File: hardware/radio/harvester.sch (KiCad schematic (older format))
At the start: 31 parts, among them U201 LTC3331

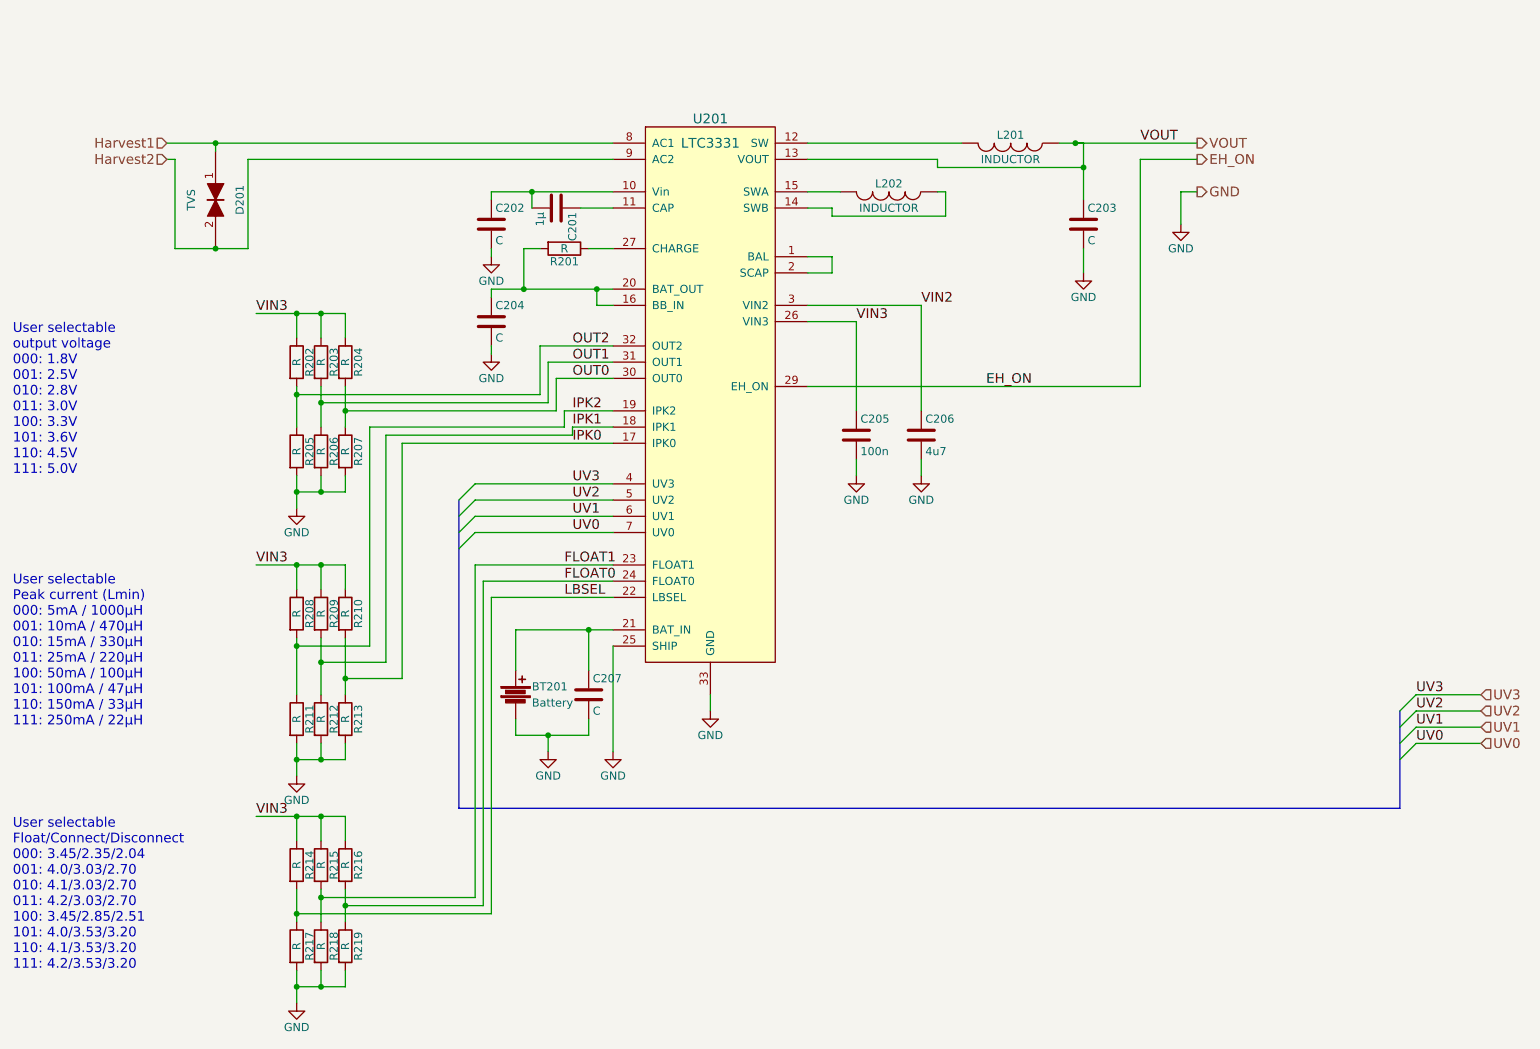
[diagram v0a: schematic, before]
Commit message: Add test points for current and voltage
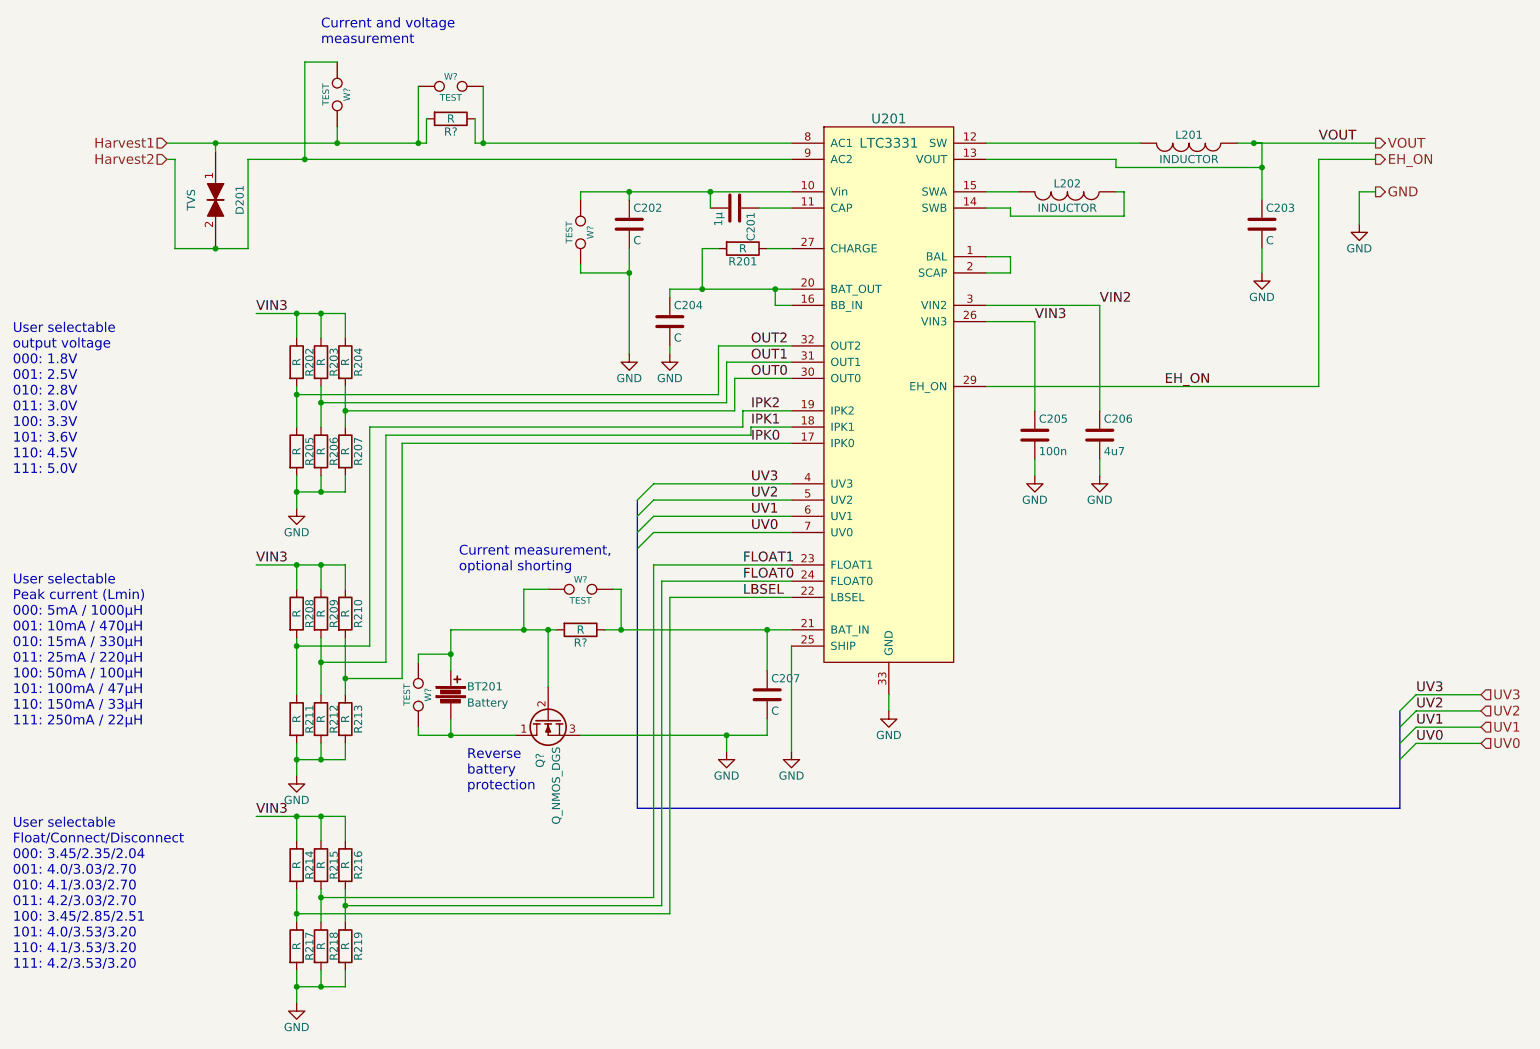
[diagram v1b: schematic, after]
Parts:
- added Q?: Q_NMOS_DGS, symbol Q_NMOS_DGS
- added R? (x2): R, symbol R
- added W? (x5): TEST, symbol TEST
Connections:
- net GND: now also Q?.3 (S), W?.2; no longer BT201.2
- net Harvest1: now also R?.2, W?.1, W?.2; no longer U201.8 (AC1)
- net Harvest2: now also W?.1
- net at C201.2, C202.1, U201.10 (Vin): now also W?.1
- net at C207.1, U201.21 (BAT_IN): now also R?.1, W?.2; no longer BT201.1
- new net: R?.1, U201.8 (AC1), W?.2
- new net: BT201.1, Q?.2 (G), R?.2, W?.1, W?.1
- new net: BT201.2, Q?.1 (D), W?.2
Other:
- note added: "Current and voltage \nmeasurement"
- note added: "Current measurement, \noptional shorting"
- note added: "Reverse \nbattery \nprotection"
- moved on the sheet: BT201, C201, C202, C203, C204, C205, C206, C207, L201, L202, R201, U201

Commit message: Assign testpoint footprints
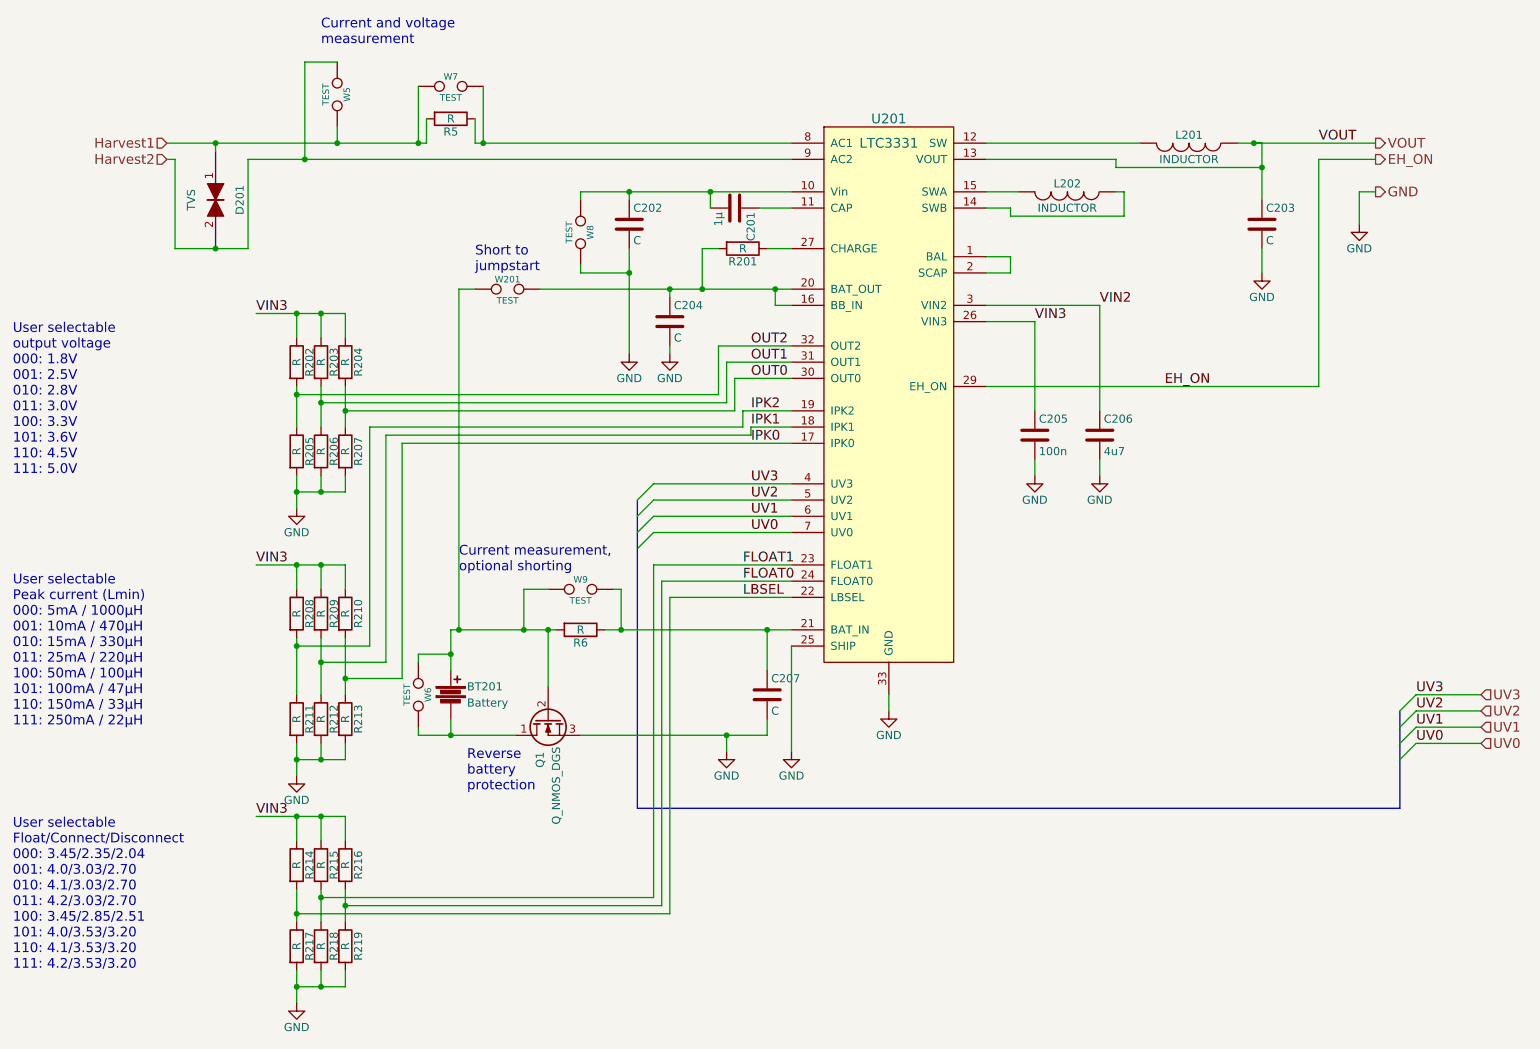
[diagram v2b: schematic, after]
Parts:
- added W201: TEST, footprints_:Test_pair_TH_small, symbol TEST
- BT201: footprint (none) -> footprints_:BLE113
- C201, C202, C203, C204, C205, C206, C207: footprint (none) -> Capacitors_SMD:C_0603
- D201: footprint (none) -> Diodes_SMD:SOD-323
- L201, L202: footprint (none) -> Resistors_SMD:R_1206
- R201, R202, R203, R204, R205, R206, R207, R208, R209, R210, R211, R212, R213, R214, R215, R216, R217, R218, R219, U201: footprint (none) -> Resistors_SMD:R_0603
- R5, R6: renamed from R?; footprint (none) -> Resistors_SMD:R_0603
- W5, W6, W8: renamed from W?; footprint (none) -> footprints_:Test_pair_TH_tiny
- W7, W9: renamed from W?; footprint (none) -> footprints_:Test_pair_TH_small
- gave numbers to parts that had none: 1
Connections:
- net at C204.1, R201.2, U201.16 (BB_IN)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: now also W201.2
- net at BT201.1, Q1.2 (G), R6.2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: now also W201.1
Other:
- note added: "Short to\njumpstart"

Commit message: Assign Q1 footprint
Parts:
- Q1: footprint (none) -> TO_SOT_Packages_SMD:SOT-23
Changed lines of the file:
@@
 F 0 "Q1" H 4700 5800 50  0000 R CNN
 F 1 "Q_NMOS_DGS" H 5050 5700 50  0000 R CNN
-F 2 "" H 4600 5850 29  0001 C CNN
+F 2 "TO_SOT_Packages_SMD:SOT-23" H 4600 5850 29  0001 C CNN
 F 3 "" H 4400 5750 60  0000 C CNN
 	1    4400 5750

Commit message: Parts placed
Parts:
- removed W5: TEST, footprints_:Test_pair_TH_tiny, symbol TEST

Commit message: Change inductor footprints to 1210
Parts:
- BT201: footprint footprints_:BLE113 -> footprints_:CR2032-holder-S8421R
- L201, L202: footprint Resistors_SMD:R_1206 -> Resistors_SMD:R_1210
- U201: footprint Resistors_SMD:R_0603 -> Housings_DFN_QFN:QFN-32-1EP_5x5mm_Pitch0.5mm
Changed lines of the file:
@@
 F 0 "U201" H 6500 4350 60  0000 C CNN
 F 1 "LTC3331" H 6500 4200 60  0000 C CNN
-F 2 "Resistors_SMD:R_0603" H 6500 1750 60  0001 C CNN
+F 2 "Housings_DFN_QFN:QFN-32-1EP_5x5mm_Pitch0.5mm" H 6500 1750 60  0001 C CNN
 F 3 "" H 6500 1750 60  0000 C CNN
 	1    6500 3200
@@
 F 0 "L202" V 7550 2500 50  0000 C CNN
 F 1 "INDUCTOR" V 7700 2500 50  0000 C CNN
-F 2 "Resistors_SMD:R_1206" H 7600 2500 60  0001 C CNN
+F 2 "Resistors_SMD:R_1210" H 7600 2500 60  0001 C CNN
 F 3 "" H 7600 2500 60  0000 C CNN
 	1    7600 2500
@@
 F 0 "L201" V 8300 2200 50  0000 C CNN
 F 1 "INDUCTOR" V 8450 2200 50  0000 C CNN
-F 2 "Resistors_SMD:R_1206" H 8350 2200 60  0001 C CNN
+F 2 "Resistors_SMD:R_1210" H 8350 2200 60  0001 C CNN
 F 3 "" H 8350 2200 60  0000 C CNN
 	1    8350 2200
@@
 F 0 "BT201" H 3900 5650 50  0000 L CNN
 F 1 "Battery" H 3900 5550 50  0000 L CNN
-F 2 "footprints_:BLE113" V 3800 5640 60  0001 C CNN
+F 2 "footprints_:CR2032-holder-S8421R" V 3800 5640 60  0001 C CNN
 F 3 "" V 3800 5640 60  0000 C CNN
 	1    3800 5600

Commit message: Routing finalized
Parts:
- removed Q1: Q_NMOS_DGS, TO_SOT_Packages_SMD:SOT-23, symbol Q_NMOS_DGS
- added Q201: BSH105, symbol Q_NMOS_GSD
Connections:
- net GND: now also Q201.2 (S)
- net VIN3: no longer R214.1, R215.1, R216.1
- net BB_IN: now reaches C204.1, R201.2, U201.16 (BB_IN), U201.20 (BAT_OUT), W201.2
- net BB_IN: now also R214.1, R215.1, R216.1
- net at BT201.1, R6.2, W201.1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: now also Q201.1 (G)
- net at BT201.2, W6.2: now also Q201.3 (D)
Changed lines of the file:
@@
 $EndComp
 $Comp
-L GND #PWR014
+L GND #PWR013
 U 1 1 55E9B04F
 P 4900 3500
-F 0 "#PWR014" H 4900 3250 50  0001 C CNN
+F 0 "#PWR013" H 4900 3250 50  0001 C CNN
 F 1 "GND" H 4900 3350 50  0000 C CNN
 F 2 "" H 4900 3500 60  0000 C CNN
@@
 $EndComp
 $Comp
-L GND #PWR015
+L GND #PWR014
 U 1 1 55E9B130
 P 5150 3500
-F 0 "#PWR015" H 5150 3250 50  0001 C CNN
+F 0 "#PWR014" H 5150 3250 50  0001 C CNN
 F 1 "GND" H 5150 3350 50  0000 C CNN
 F 2 "" H 5150 3500 60  0000 C CNN
@@
 VIN3
 $Comp
-L GND #PWR016
+L GND #PWR015
 U 1 1 55E9B68B
 P 2850 4450
-F 0 "#PWR016" H 2850 4200 50  0001 C CNN
+F 0 "#PWR015" H 2850 4200 50  0001 C CNN
 F 1 "GND" H 2850 4300 50  0000 C CNN
 F 2 "" H 2850 4450 60  0000 C CNN
@@
 	1    0    0    -1
 $EndComp
-Text Label 2600 6350 0    60   ~ 0
-VIN3
-$Comp
-L GND #PWR017
+$Comp
+L GND #PWR016
 U 1 1 55E9C430
 P 2850 7500
-F 0 "#PWR017" H 2850 7250 50  0001 C CNN
+F 0 "#PWR016" H 2850 7250 50  0001 C CNN
 F 1 "GND" H 2850 7350 50  0000 C CNN
 F 2 "" H 2850 7500 60  0000 C CNN
@@
 $EndComp
 $Comp
-L GND #PWR018
+L GND #PWR017
 U 1 1 55E9C656
 P 5900 5950
-F 0 "#PWR018" H 5900 5700 50  0001 C CNN
+F 0 "#PWR017" H 5900 5700 50  0001 C CNN
 F 1 "GND" H 5900 5800 50  0000 C CNN
 F 2 "" H 5900 5950 60  0000 C CNN
@@
 VIN3
 $Comp
-L GND #PWR019
+L GND #PWR018
 U 1 1 55E9DB9C
 P 2850 6100
-F 0 "#PWR019" H 2850 5850 50  0001 C CNN
+F 0 "#PWR018" H 2850 5850 50  0001 C CNN
 F 1 "GND" H 2850 5950 50  0000 C CNN
 F 2 "" H 2850 6100 60  0000 C CNN
@@
 UV0
 $Comp
-L GND #PWR020
+L GND #PWR019
 U 1 1 55E9FF2E
 P 6500 5700
-F 0 "#PWR020" H 6500 5450 50  0001 C CNN
+F 0 "#PWR019" H 6500 5450 50  0001 C CNN
 F 1 "GND" H 6500 5550 50  0000 C CNN
 F 2 "" H 6500 5700 60  0000 C CNN
@@
 $EndComp
 $Comp
-L GND #PWR021
+L GND #PWR020
 U 1 1 55EA0A97
 P 8800 3000
-F 0 "#PWR021" H 8800 2750 50  0001 C CNN
+F 0 "#PWR020" H 8800 2750 50  0001 C CNN
 F 1 "GND" H 8800 2850 50  0000 C CNN
 F 2 "" H 8800 3000 60  0000 C CNN
@@
 $EndComp
 $Comp
-L GND #PWR022
+L GND #PWR021
 U 1 1 55EA354D
 P 7800 4250
-F 0 "#PWR022" H 7800 4000 50  0001 C CNN
+F 0 "#PWR021" H 7800 4000 50  0001 C CNN
 F 1 "GND" H 7800 4100 50  0000 C CNN
 F 2 "" H 7800 4250 60  0000 C CNN
@@
 $EndComp
 $Comp
-L GND #PWR023
+L GND #PWR022
 U 1 1 55EA359B
 P 7400 4250
-F 0 "#PWR023" H 7400 4000 50  0001 C CNN
+F 0 "#PWR022" H 7400 4000 50  0001 C CNN
 F 1 "GND" H 7400 4100 50  0000 C CNN
 F 2 "" H 7400 4250 60  0000 C CNN
@@
 $EndComp
 $Comp
-L GND #PWR024
+L GND #PWR023
 U 1 1 55EA7D40
 P 5500 5950
-F 0 "#PWR024" H 5500 5700 50  0001 C CNN
+F 0 "#PWR023" H 5500 5700 50  0001 C CNN
 F 1 "GND" H 5500 5800 50  0000 C CNN
 F 2 "" H 5500 5950 60  0000 C CNN
@@
 $EndComp
 $Comp
-L GND #PWR025
+L GND #PWR024
 U 1 1 55EB3C4E
 P 9400 2700
-F 0 "#PWR025" H 9400 2450 50  0001 C CNN
+F 0 "#PWR024" H 9400 2450 50  0001 C CNN
 F 1 "GND" H 9400 2550 50  0000 C CNN
 F 2 "" H 9400 2700 60  0000 C CNN
@@
 Text HLabel 9500 2500 2    60   Output ~ 0
 GND
-$Comp
-L Q_NMOS_DGS Q1
-U 1 1 55F1D0B7
-P 4400 5750
-F 0 "Q1" H 4700 5800 50  0000 R CNN
-F 1 "Q_NMOS_DGS" H 5050 5700 50  0000 R CNN
-F 2 "TO_SOT_Packages_SMD:SOT-23" H 4600 5850 29  0001 C CNN
-F 3 "" H 4400 5750 60  0000 C CNN
-	1    4400 5750
-	0    -1   1    0
-$EndComp
 Text Notes 3900 6200 0    60   ~ 0
 Reverse \nbattery \nprotection
@@
 	0    1    1    0
 $EndComp
+$Comp
+L Q_NMOS_GSD Q201
+U 1 1 55F70C9A
+P 4400 5750
+F 0 "Q201" H 4700 5800 50  0000 R CNN
+F 1 "BSH105" H 5050 5700 50  0000 R CNN
+F 2 "" H 4600 5850 29  0000 C CNN
+F 3 "" H 4400 5750 60  0000 C CNN
+	1    4400 5750
+	0    -1   1    0
+$EndComp
+Text Label 4400 3100 0    60   ~ 0
+BB_IN
+Text Label 2600 6350 0    60   ~ 0
+BB_IN
 $EndSCHEMATC

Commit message: Add revision information
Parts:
- L201, L202: value INDUCTOR -> AISC-1210HS-220K-T2
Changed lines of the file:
@@
 Sheet 2 5
 Title "Energy harvesting sensor board with BLE radio"
-Date "2015-09-08"
-Rev "e6b12b6"
+Date "2015-09-14"
+Rev "bff4fab"
 Comp "Aalto University / Otso Jousimaa"
-Comment1 "First draft for review"
+Comment1 "First production draft"
 Comment2 ""
 Comment3 ""
@@
 P 7600 2500
 F 0 "L202" V 7550 2500 50  0000 C CNN
-F 1 "INDUCTOR" V 7700 2500 50  0000 C CNN
+F 1 "AISC-1210HS-220K-T2" V 7850 2500 50  0000 C CNN
 F 2 "Resistors_SMD:R_1210" H 7600 2500 60  0001 C CNN
 F 3 "" H 7600 2500 60  0000 C CNN
@@
 P 8350 2200
 F 0 "L201" V 8300 2200 50  0000 C CNN
-F 1 "INDUCTOR" V 8450 2200 50  0000 C CNN
+F 1 "AISC-1210HS-220K-T2" V 8200 2200 50  0000 C CNN
 F 2 "Resistors_SMD:R_1210" H 8350 2200 60  0001 C CNN
 F 3 "" H 8350 2200 60  0000 C CNN
